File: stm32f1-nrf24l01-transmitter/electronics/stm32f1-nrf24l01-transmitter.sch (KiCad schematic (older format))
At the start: 28 parts, among them K1 CONN_3, K10 CONN_3, K11 CONN_3, K12 CONN_3, K2 CONN_3, K3 CONN_3, K4 CONN_3, K5 CONN_3, K6 CONN_3, K7 CONN_3, K8 CONN_3, K9 CONN_3, P1 Charge, P2 LED, P3 CONN_2, P4 CONN_2, Q1 BC548, SW1 ON/OFF, U1 LIPO_CHARGER_+_PROTECTION, U2 STM32F103C8T6_DEV_BOARD, U3 NRF24L01P

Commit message: Tweak schematics
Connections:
- net at U2.20 (3V3): now also U2.21 (VB)
- no-connect marks 14 -> 12
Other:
- note added: "TIM2_CH1"
- note removed: "What to do with VB?"
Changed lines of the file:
@@
 $EndDescr
-$Comp
-L STM32F103C8T6_DEV_BOARD U2
-U 1 1 57202BC2
-P 5850 3000
-F 0 "U2" H 4850 4500 60  0000 L CNN
-F 1 "STM32F103C8T6_DEV_BOARD" H 6800 1300 60  0000 C CNN
-F 2 "~" H 6000 3400 60  0000 C CNN
-F 3 "~" H 6000 3400 60  0000 C CNN
-	1    5850 3000
-	1    0    0    -1
-$EndComp
 $Comp
 L NRF24L01P U3
@@
 	1    0    0    -1
 $EndComp
-Text Notes 5550 800  0    60   ~ 0
-What to do with VB?
 $Comp
 L C C1
@@
 Wire Wire Line
 	9850 2550 9850 2700
-NoConn ~ 5850 1250
 Wire Wire Line
 	2450 1150 1650 1150
@@
 Wire Wire Line
 	6400 1150 6400 1250
-NoConn ~ 6200 1250
+Text Notes 4050 3850 0    60   ~ 0
+TIM2_CH1
+$Comp
+L STM32F103C8T6_DEV_BOARD U2
+U 1 1 57202BC2
+P 5850 3000
+F 0 "U2" H 4850 4500 60  0000 L CNN
+F 1 "STM32F103C8T6_DEV_BOARD" H 6800 1300 60  0000 C CNN
+F 2 "~" H 6000 3400 60  0000 C CNN
+F 3 "~" H 6000 3400 60  0000 C CNN
+	1    5850 3000
+	1    0    0    -1
+$EndComp
+Wire Wire Line
+	5850 1250 5850 1100
+Wire Wire Line
+	5850 1100 6200 1100
+Wire Wire Line
+	6200 1100 6200 1250
 $EndSCHEMATC

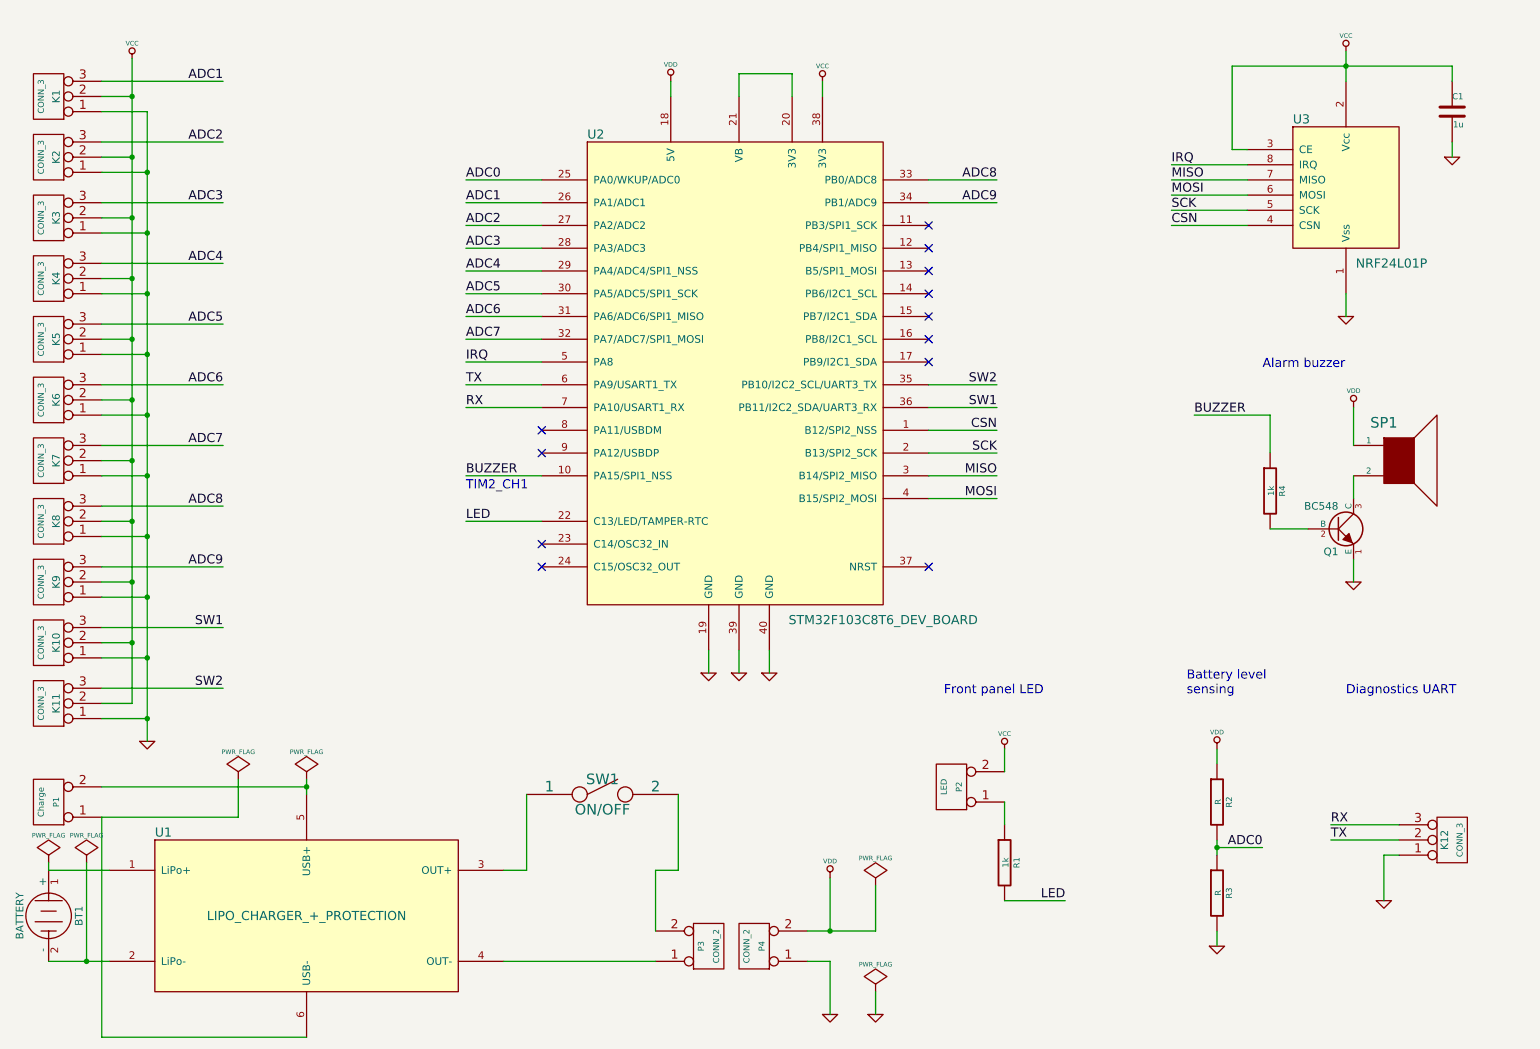
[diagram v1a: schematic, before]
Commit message: Make CE pin software controllable
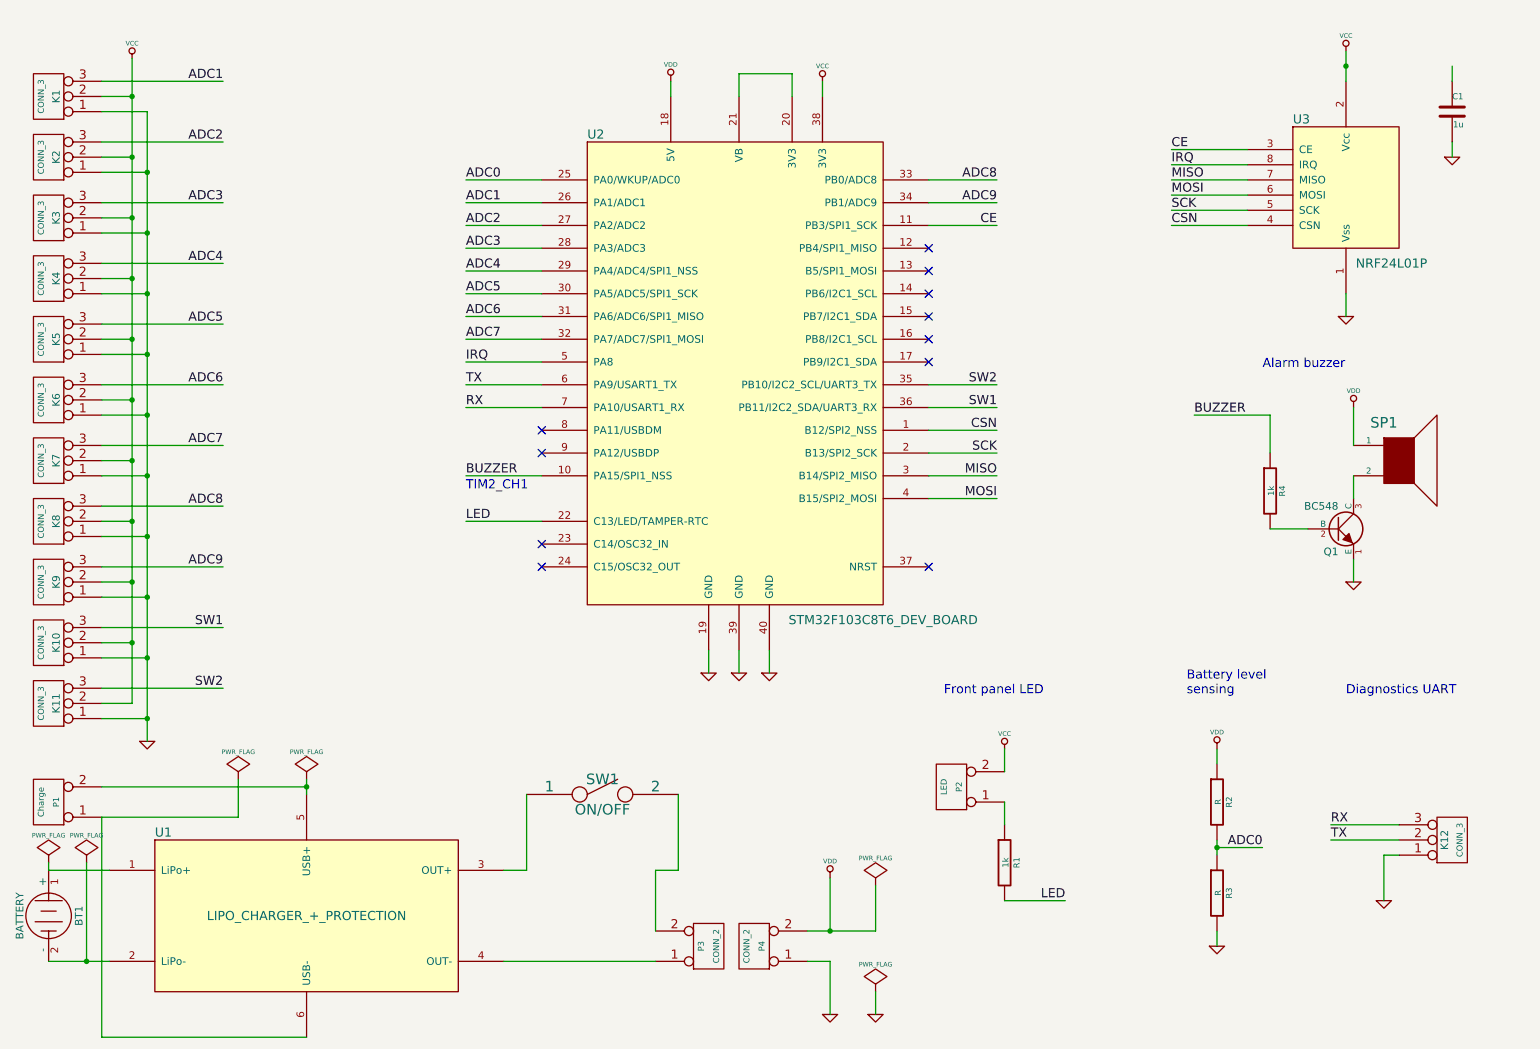
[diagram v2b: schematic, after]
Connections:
- net VCC: no longer C1.1, U3.3 (CE)
- net CE: now reaches U2.11 (PB3/SPI1_SCK)
- net CE: now also U3.3 (CE)
- no-connect marks 12 -> 11
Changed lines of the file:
@@
 Sheet 1 1
 Title "STM32F1 NRF24L01 RC transmitter"
-Date "27 apr 2016"
+Date "9 may 2016"
 Rev "1"
 Comp "LANE Boys RC"
@@
 Wire Wire Line
 	10550 1050 10550 1150
-Wire Wire Line
-	9100 1050 10550 1050
 Connection ~ 9850 1050
 Wire Wire Line
@@
 	7100 3900 7550 3900
 Wire Wire Line
-	9200 1600 9100 1600
-Wire Wire Line
-	9100 1600 9100 1050
+	9200 1600 8700 1600
 Wire Wire Line
 	9200 2100 8700 2100
@@
 	1    0    0    -1
 $EndComp
-NoConn ~ 7100 2100
 NoConn ~ 7100 2250
 NoConn ~ 7100 2400
@@
 	2450 5150 1650 5150
 Wire Wire Line
-	1650 5250 1850 5250
-Wire Wire Line
-	1850 5250 1850 1000
+	1850 5250 1650 5250
+Wire Wire Line
+	1850 1000 1850 5250
 Wire Wire Line
 	1650 4850 1850 4850
@@
 Wire Wire Line
 	6200 1100 6200 1250
+Text Label 8700 1600 0    60   ~ 0
+CE
+Wire Wire Line
+	7100 2100 7550 2100
+Text Label 7550 2100 2    60   ~ 0
+CE
 $EndSCHEMATC

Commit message: nRF24L01 CE tied to Vcc; Add smoothing cap for battery measurement
Add 4-pin socket for BT module
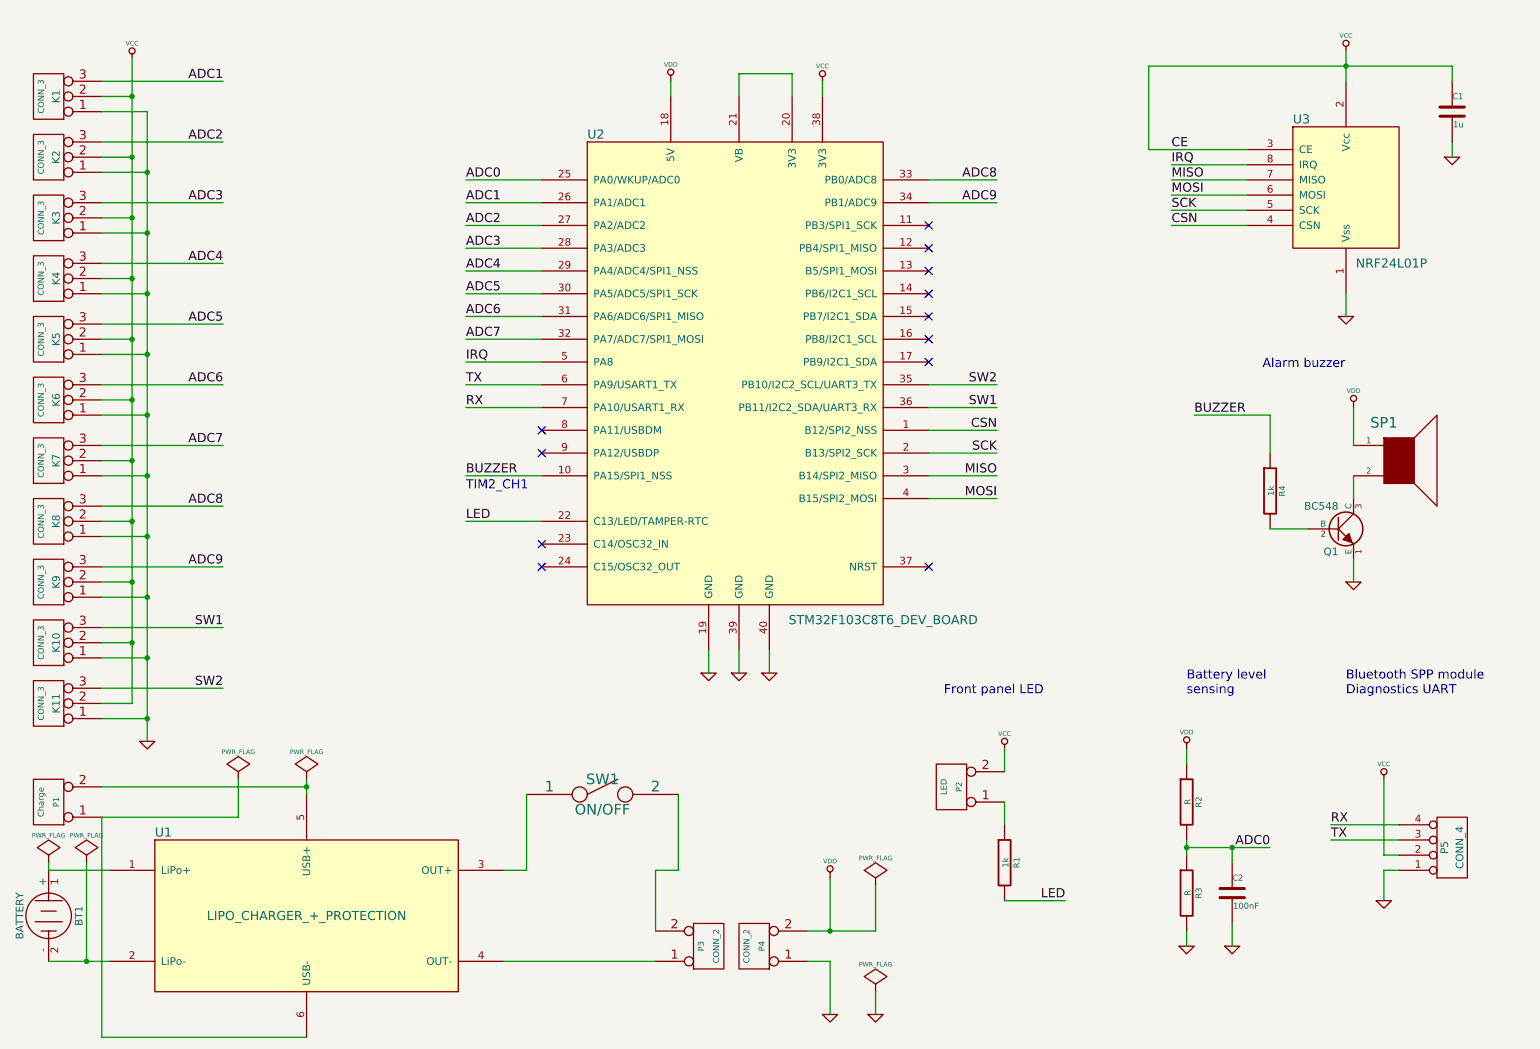
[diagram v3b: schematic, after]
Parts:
- removed K12: CONN_3, symbol CONN_3
- added C2: 100nF, ~, symbol C
- added P5: CONN_4, symbol CONN_4
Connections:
- net ADC0: now also C2.1
- net GND: now also C2.2, P5.1 (P1)
- net RX: now also P5.4 (P4)
- net TX: now also P5.3 (P3)
- net VCC: now also C1.1, U3.3 (CE), P5.2 (P2)
- net CE: no longer names the net of U2.11 (PB3/SPI1_SCK)
- net CE: no longer U3.3 (CE)
- no-connect marks 11 -> 12
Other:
- note added: "Bluetooth SPP module\nDiagnostics UART"
- note removed: "Diagnostics UART"
- moved on the sheet: R2, R3
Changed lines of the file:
@@
 Sheet 1 1
 Title "STM32F1 NRF24L01 RC transmitter"
-Date "9 may 2016"
+Date "27 may 2016"
 Rev "1"
 Comp "LANE Boys RC"
@@
 L R R2
 U 1 1 57203444
-P 9000 5900
-F 0 "R2" V 9080 5900 40  0000 C CNN
-F 1 "R" V 9007 5901 40  0000 C CNN
-F 2 "~" V 8930 5900 30  0000 C CNN
-F 3 "~" H 9000 5900 30  0000 C CNN
-	1    9000 5900
+P 8800 5900
+F 0 "R2" V 8880 5900 40  0000 C CNN
+F 1 "R" V 8807 5901 40  0000 C CNN
+F 2 "~" V 8730 5900 30  0000 C CNN
+F 3 "~" H 8800 5900 30  0000 C CNN
+	1    8800 5900
 	1    0    0    -1
 $EndComp
@@
 L R R3
 U 1 1 57203451
-P 9000 6500
-F 0 "R3" V 9080 6500 40  0000 C CNN
-F 1 "R" V 9007 6501 40  0000 C CNN
-F 2 "~" V 8930 6500 30  0000 C CNN
-F 3 "~" H 9000 6500 30  0000 C CNN
-	1    9000 6500
+P 8800 6500
+F 0 "R3" V 8880 6500 40  0000 C CNN
+F 1 "R" V 8807 6501 40  0000 C CNN
+F 2 "~" V 8730 6500 30  0000 C CNN
+F 3 "~" H 8800 6500 30  0000 C CNN
+	1    8800 6500
 	1    0    0    -1
 $EndComp
@@
 L VDD #PWR011
 U 1 1 57203459
-P 9000 5550
-F 0 "#PWR011" H 9000 5650 30  0001 C CNN
-F 1 "VDD" H 9000 5660 30  0000 C CNN
-F 2 "" H 9000 5550 60  0000 C CNN
-F 3 "" H 9000 5550 60  0000 C CNN
-	1    9000 5550
+P 8800 5550
+F 0 "#PWR011" H 8800 5650 30  0001 C CNN
+F 1 "VDD" H 8800 5660 30  0000 C CNN
+F 2 "" H 8800 5550 60  0000 C CNN
+F 3 "" H 8800 5550 60  0000 C CNN
+	1    8800 5550
 	1    0    0    -1
 $EndComp
@@
 L GND #PWR012
 U 1 1 572034AB
-P 9000 6850
-F 0 "#PWR012" H 9000 6850 30  0001 C CNN
-F 1 "GND" H 9000 6780 30  0001 C CNN
-F 2 "" H 9000 6850 60  0000 C CNN
-F 3 "" H 9000 6850 60  0000 C CNN
-	1    9000 6850
-	1    0    0    -1
-$EndComp
-Text Label 9300 6200 2    60   ~ 0
+P 8800 6850
+F 0 "#PWR012" H 8800 6850 30  0001 C CNN
+F 1 "GND" H 8800 6780 30  0001 C CNN
+F 2 "" H 8800 6850 60  0000 C CNN
+F 3 "" H 8800 6850 60  0000 C CNN
+	1    8800 6850
+	1    0    0    -1
+$EndComp
+Text Label 9350 6200 2    60   ~ 0
 ADC0
 Text Notes 8800 5200 0    60   ~ 0
@@
 	7100 3900 7550 3900
 Wire Wire Line
-	9200 1600 8700 1600
+	8550 1600 9200 1600
 Wire Wire Line
 	9200 2100 8700 2100
@@
 	4550 4050 4050 4050
 Wire Wire Line
-	9000 5550 9000 5650
-Wire Wire Line
-	9000 6150 9000 6250
-Wire Wire Line
-	9000 6750 9000 6850
-Wire Wire Line
-	9000 6200 9300 6200
-Connection ~ 9000 6200
+	8800 5550 8800 5650
+Wire Wire Line
+	8800 6150 8800 6250
+Wire Wire Line
+	8800 6750 8800 6850
+Wire Wire Line
+	8800 6200 9350 6200
+Connection ~ 8800 6200
 Wire Wire Line
 	4550 1800 4050 1800
@@
 SW1
 $Comp
-L CONN_3 K12
-U 1 1 57204ABA
-P 10550 6150
-F 0 "K12" V 10500 6150 50  0000 C CNN
-F 1 "CONN_3" V 10600 6150 40  0000 C CNN
-F 2 "" H 10550 6150 60  0000 C CNN
-F 3 "" H 10550 6150 60  0000 C CNN
-	1    10550 6150
-	1    0    0    1
-$EndComp
-$Comp
 L GND #PWR015
 U 1 1 57204AD8
@@
 $EndComp
 Wire Wire Line
-	10200 6250 10100 6250
-Wire Wire Line
-	10100 6250 10100 6550
-Wire Wire Line
 	10200 6150 9750 6150
 Wire Wire Line
@@
 TX
 Text Notes 9850 5200 0    60   ~ 0
-Diagnostics UART
+Bluetooth SPP module\nDiagnostics UART
 Wire Wire Line
 	4050 3150 4550 3150
@@
 Text Label 8700 1600 0    60   ~ 0
 CE
-Wire Wire Line
-	7100 2100 7550 2100
-Text Label 7550 2100 2    60   ~ 0
-CE
+NoConn ~ 7100 2100
+Wire Wire Line
+	8550 1050 10550 1050
+Wire Wire Line
+	8550 1050 8550 1600
+$Comp
+L C C2
+U 1 1 5747F7DC
+P 9100 6500
+F 0 "C2" H 9100 6600 40  0000 L CNN
+F 1 "100nF" H 9106 6415 40  0000 L CNN
+F 2 "~" H 9138 6350 30  0000 C CNN
+F 3 "~" H 9100 6500 60  0000 C CNN
+	1    9100 6500
+	1    0    0    -1
+$EndComp
+Wire Wire Line
+	9100 6300 9100 6200
+Connection ~ 9100 6200
+$Comp
+L GND #PWR026
+U 1 1 5747F906
+P 9100 6850
+F 0 "#PWR026" H 9100 6850 30  0001 C CNN
+F 1 "GND" H 9100 6780 30  0001 C CNN
+F 2 "" H 9100 6850 60  0000 C CNN
+F 3 "" H 9100 6850 60  0000 C CNN
+	1    9100 6850
+	1    0    0    -1
+$EndComp
+Wire Wire Line
+	9100 6700 9100 6850
+$Comp
+L CONN_4 P5
+U 1 1 5747FB60
+P 10550 6200
+F 0 "P5" V 10500 6200 50  0000 C CNN
+F 1 "CONN_4" V 10600 6200 50  0000 C CNN
+F 2 "" H 10550 6200 60  0000 C CNN
+F 3 "" H 10550 6200 60  0000 C CNN
+	1    10550 6200
+	1    0    0    1
+$EndComp
+Wire Wire Line
+	10200 6350 10100 6350
+Wire Wire Line
+	10100 6350 10100 6550
+$Comp
+L VCC #PWR027
+U 1 1 5747FC1F
+P 10100 5750
+F 0 "#PWR027" H 10100 5850 30  0001 C CNN
+F 1 "VCC" H 10100 5850 30  0000 C CNN
+F 2 "" H 10100 5750 60  0000 C CNN
+F 3 "" H 10100 5750 60  0000 C CNN
+	1    10100 5750
+	1    0    0    -1
+$EndComp
+Wire Wire Line
+	10200 6250 10100 6250
+Wire Wire Line
+	10100 6250 10100 5750
 $EndSCHEMATC

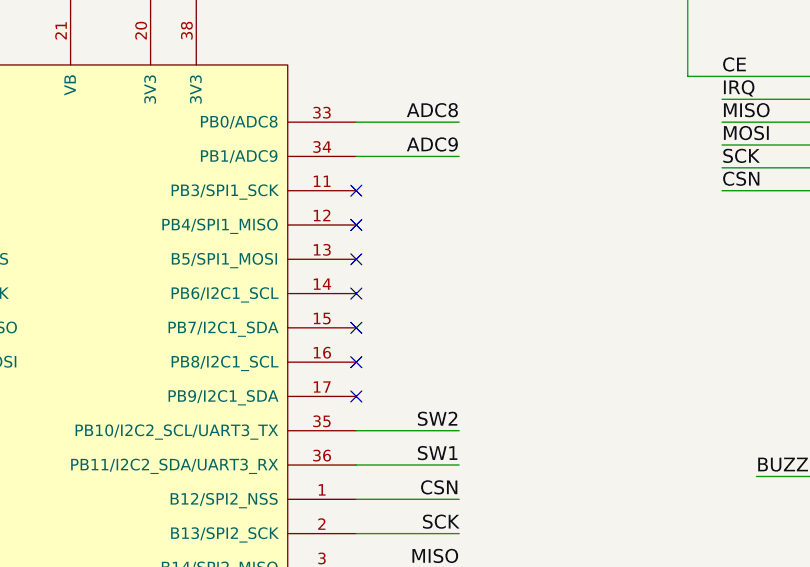
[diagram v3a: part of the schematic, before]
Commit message: Add unused inputs as switches and configure them as inputs
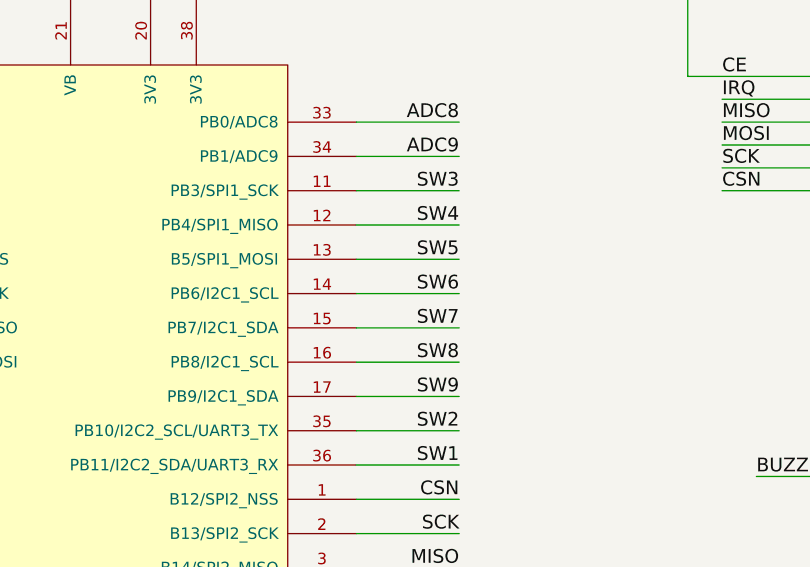
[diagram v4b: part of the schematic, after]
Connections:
- net SW3: now reaches U2.11 (PB3/SPI1_SCK)
- net SW4: now reaches U2.12 (PB4/SPI1_MISO)
- net SW5: now reaches U2.13 (B5/SPI1_MOSI)
- net SW6: now reaches U2.14 (PB6/I2C1_SCL)
- net SW7: now reaches U2.15 (PB7/I2C1_SDA)
- net SW8: now reaches U2.16 (PB8/I2C1_SCL)
- net SW9: now reaches U2.17 (PB9/I2C1_SDA)
- no-connect marks 12 -> 5
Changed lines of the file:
@@
 EESchema Schematic File Version 2
-LIBS:WLA-STM32
-LIBS:WLA-nrf24
-LIBS:WLA-power
 LIBS:power
 LIBS:device
@@
 Sheet 1 1
 Title "STM32F1 NRF24L01 RC transmitter"
-Date "27 may 2016"
+Date "12 jun 2016"
 Rev "1"
 Comp "LANE Boys RC"
@@
 	1    0    0    -1
 $EndComp
-NoConn ~ 7100 2250
-NoConn ~ 7100 2400
-NoConn ~ 7100 2550
-NoConn ~ 7100 2700
-NoConn ~ 7100 2850
-NoConn ~ 7100 3000
 NoConn ~ 4550 3450
 NoConn ~ 4550 3600
@@
 Text Label 8700 1600 0    60   ~ 0
 CE
-NoConn ~ 7100 2100
 Wire Wire Line
 	8550 1050 10550 1050
@@
 Wire Wire Line
 	10100 6250 10100 5750
+Wire Wire Line
+	7550 2100 7100 2100
+Wire Wire Line
+	7550 2250 7100 2250
+Wire Wire Line
+	7550 2400 7100 2400
+Wire Wire Line
+	7550 2550 7100 2550
+Wire Wire Line
+	7550 2700 7100 2700
+Wire Wire Line
+	7550 2850 7100 2850
+Wire Wire Line
+	7550 3000 7100 3000
+Text Label 7550 2100 2    60   ~ 0
+SW3
+Text Label 7550 2250 2    60   ~ 0
+SW4
+Text Label 7550 2400 2    60   ~ 0
+SW5
+Text Label 7550 2550 2    60   ~ 0
+SW6
+Text Label 7550 2700 2    60   ~ 0
+SW7
+Text Label 7550 2850 2    60   ~ 0
+SW8
+Text Label 7550 3000 2    60   ~ 0
+SW9
 $EndSCHEMATC
